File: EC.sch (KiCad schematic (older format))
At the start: 28 parts, among them J10 RS232, J2 MICROSD, J6 DEBUG, J8 DEBUG, Q12 FK3303010L, Q13 FK3303010L, SW3 SW-DIP-4, U10 MAX3232PW, U9 NUF2042XV6

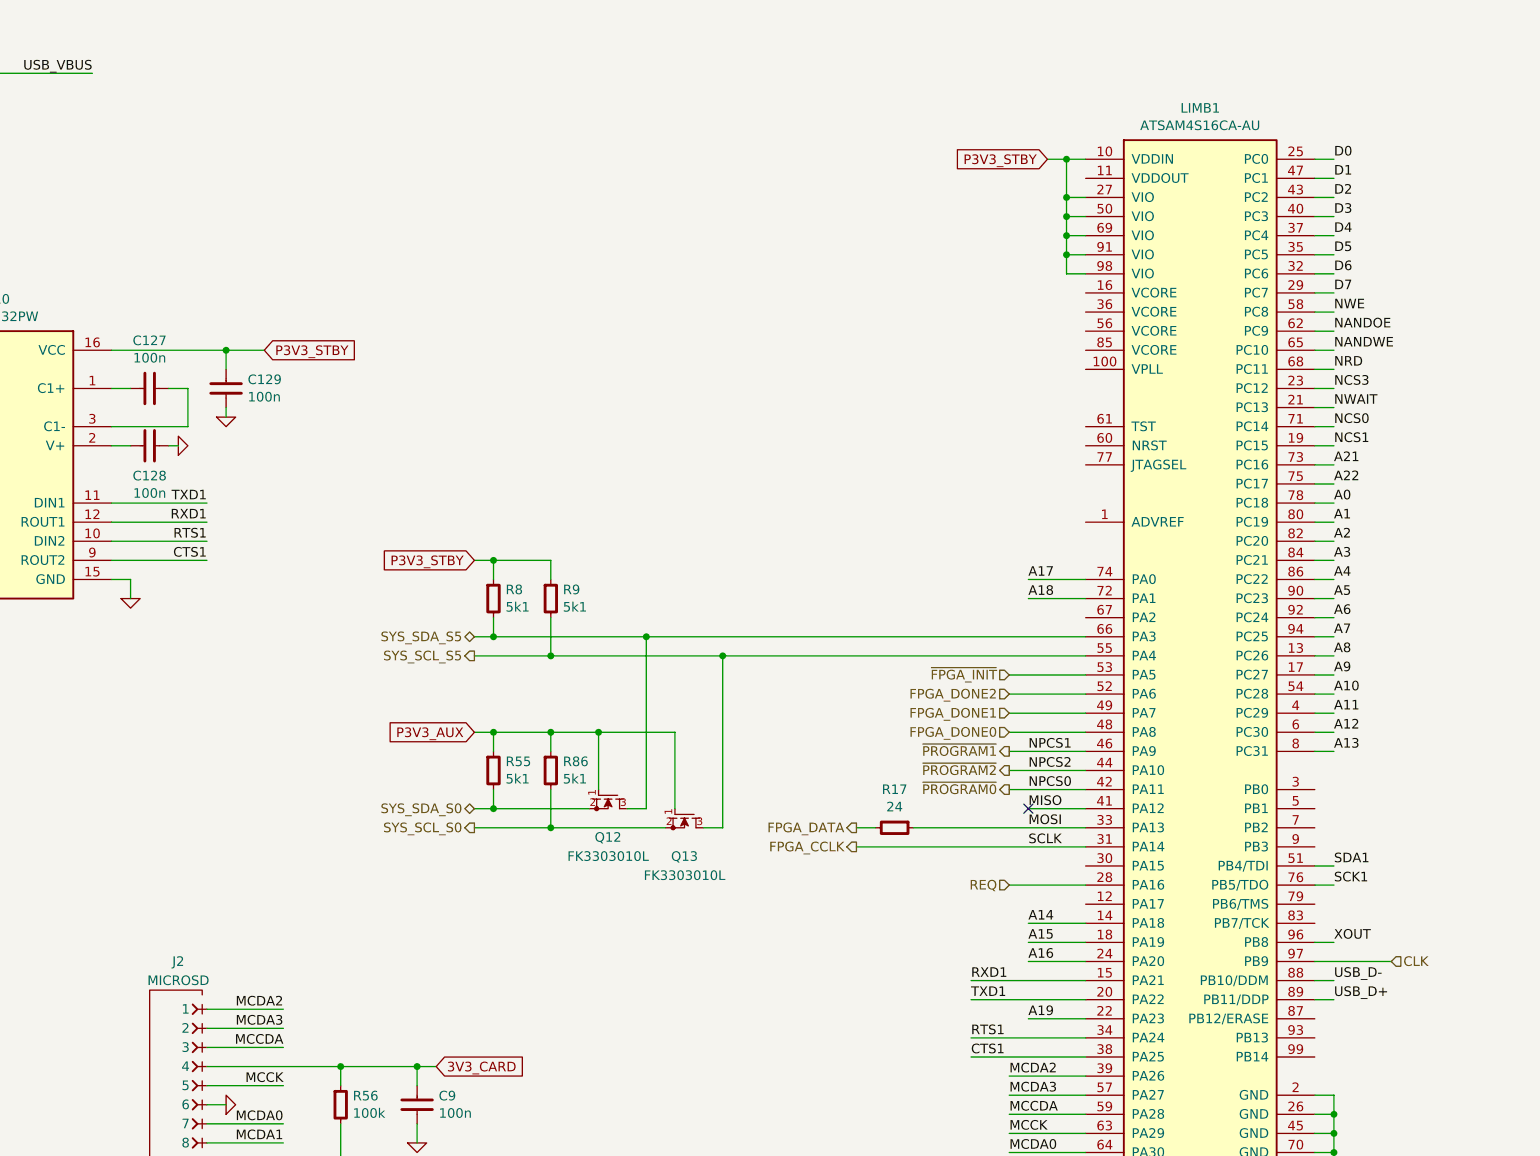
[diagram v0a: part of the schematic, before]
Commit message: Add CPU fan
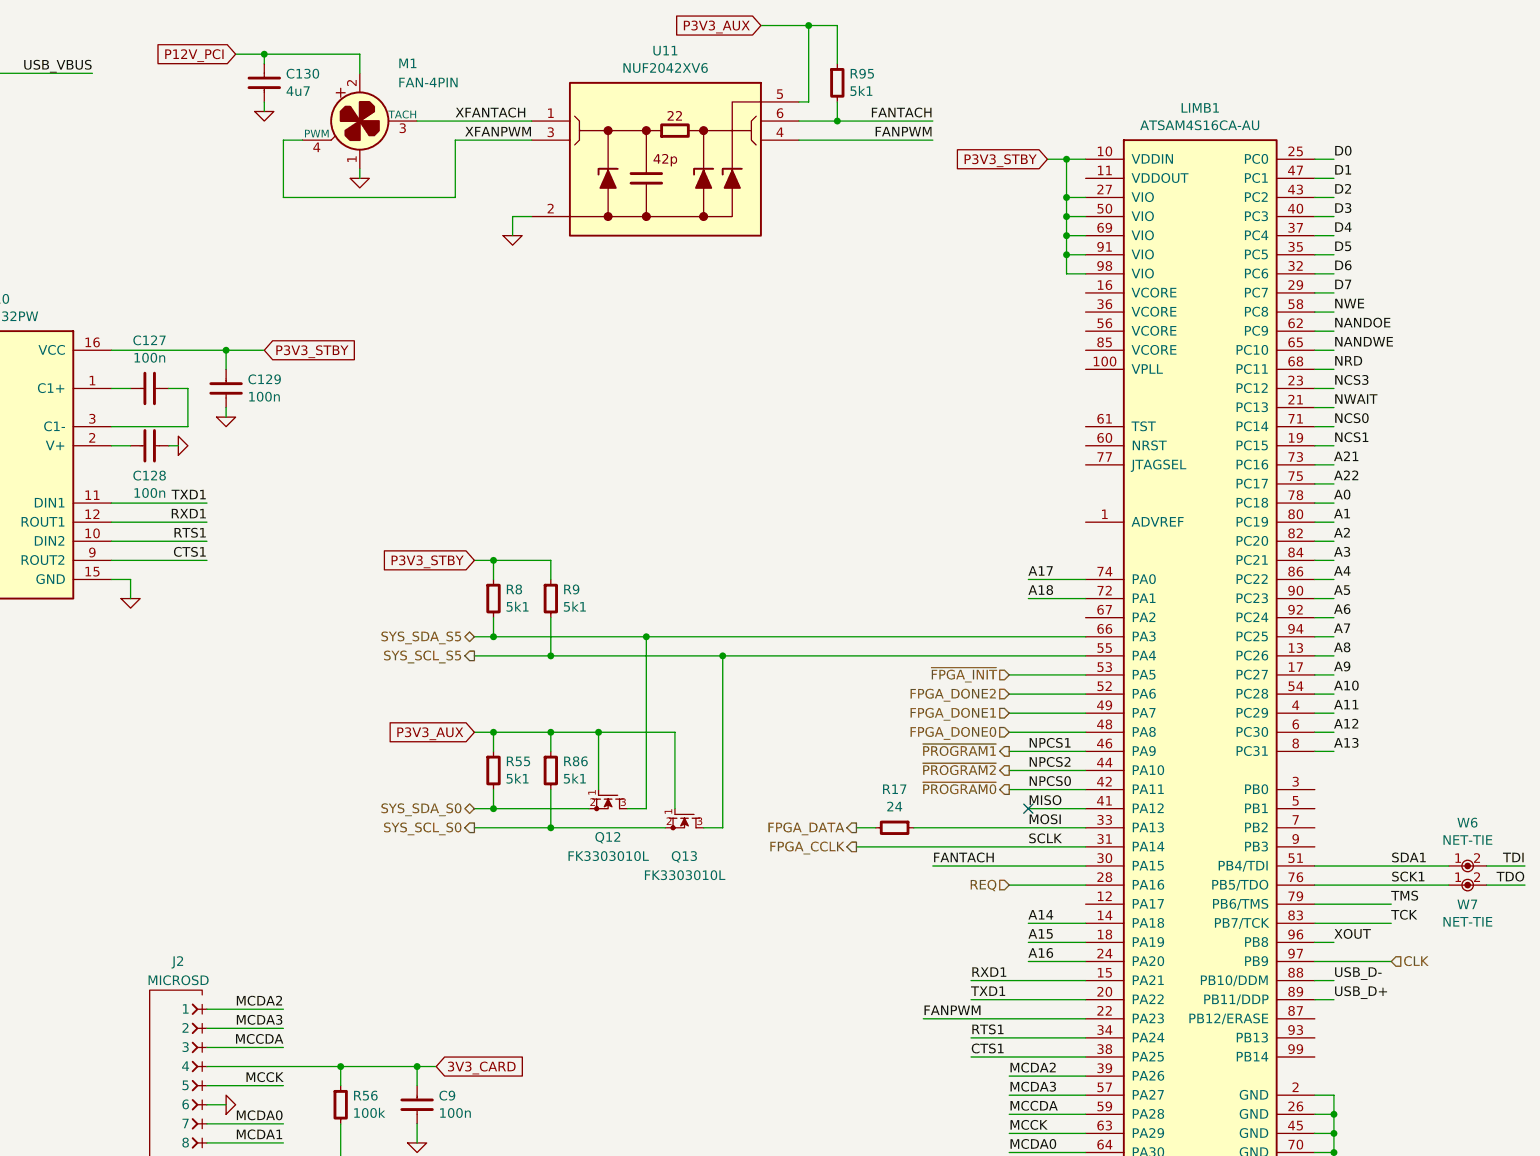
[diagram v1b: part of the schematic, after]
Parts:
- added C130: 4u7, IPC7351-Nominal:CAPC3216X70, symbol C-1206
- added M1: FAN-4PIN, conn-100mil:CONN-100MIL-M-1x4-SHROUD, symbol FAN-4PIN
- added R95: 5k1, IPC7351-Nominal:RESC1005X40, symbol R-0402
- added U11: NUF2042XV6, smd-semi:SOT-563, symbol NUF2042XV6
- added W6, W7: NET-TIE, conn-test:NET-TIE-0.2mm, symbol NET-TIE
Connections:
- net labels added: FANPWM, FANTACH, P12V_PCI, XFANPWM, XFANTACH
- net labels removed: A19
- wire segments 191 -> 216
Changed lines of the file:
@@
 Text Label 9000 3700 0    50   ~ 0
 A18
-Text Label 9000 5900 0    50   ~ 0
-A19
 Text Label 10600 3000 0    50   ~ 0
 A21
@@
 Text Label 8900 6300 0    50   ~ 0
 MCDA3
-Text Label 10600 5200 0    50   ~ 0
+Text Label 10900 5200 0    50   ~ 0
 SCK1
-Text Label 10600 5100 0    50   ~ 0
+Text Label 10900 5100 0    50   ~ 0
 SDA1
 Text Label 10600 5800 0    50   ~ 0
@@
 	8700 5800 9300 5800
 Wire Wire Line
-	9000 5900 9300 5900
+	8450 5900 9300 5900
 Wire Wire Line
 	8700 6000 9300 6000
@@
 	10500 4500 10600 4500
 Wire Wire Line
-	10500 5100 10600 5100
-Wire Wire Line
-	10500 5200 10600 5200
+	10500 5100 11200 5100
+Wire Wire Line
+	10500 5200 11200 5200
 Wire Wire Line
 	10600 5500 10500 5500
@@
 	10600 5800 10500 5800
 $Comp
-L GND #PWR137
+L GND #PWR140
 U 1 1 577EAB82
 P 10600 6800
-F 0 "#PWR137" H 10600 6800 30  0001 C CNN
+F 0 "#PWR140" H 10600 6800 30  0001 C CNN
 F 1 "GND" H 10600 6730 30  0001 C CNN
 F 2 "" H 10600 6800 60  0000 C CNN
@@
 Connection ~ 5800 6150
 $Comp
-L GND #PWR136
+L GND #PWR138
 U 1 1 577EEC84
 P 5800 6550
-F 0 "#PWR136" H 5800 6550 30  0001 C CNN
+F 0 "#PWR138" H 5800 6550 30  0001 C CNN
 F 1 "GND" H 5800 6480 30  0001 C CNN
 F 2 "" H 5800 6550 60  0000 C CNN
@@
 Wire Wire Line
 	4200 3400 4700 3400
+$Comp
+L NET-TIE W6
+U 1 1 57A3DAE4
+P 11300 5100
+F 0 "W6" H 11300 5325 50  0000 C CNN
+F 1 "NET-TIE" H 11300 5234 50  0000 C CNN
+F 2 "conn-test:NET-TIE-0.2mm" H 11300 5000 50  0001 C CNN
+F 3 "" H 11300 5100 60  0000 C CNN
+	1    11300 5100
+	1    0    0    -1
+$EndComp
+Text Label 11600 5100 2    50   ~ 0
+TDI
+Wire Wire Line
+	11600 5100 11400 5100
+$Comp
+L NET-TIE W7
+U 1 1 57A3DF12
+P 11300 5200
+F 0 "W7" H 11300 5097 50  0000 C CNN
+F 1 "NET-TIE" H 11300 5006 50  0000 C CNN
+F 2 "conn-test:NET-TIE-0.2mm" H 11300 5100 50  0001 C CNN
+F 3 "" H 11300 5200 60  0000 C CNN
+	1    11300 5200
+	1    0    0    -1
+$EndComp
+Text Label 11600 5200 2    50   ~ 0
+TDO
+Wire Wire Line
+	11600 5200 11400 5200
+Text Label 10900 5300 0    50   ~ 0
+TMS
+Wire Wire Line
+	10900 5300 10500 5300
+Text Label 10900 5400 0    50   ~ 0
+TCK
+Wire Wire Line
+	10900 5400 10500 5400
+$Comp
+L FAN-4PIN M1
+U 1 1 57A3FD69
+P 5500 1200
+F 0 "M1" H 5700 1500 50  0000 L CNN
+F 1 "FAN-4PIN" H 5700 1400 50  0000 L CNN
+F 2 "conn-100mil:CONN-100MIL-M-1x4-SHROUD" H 5841 1109 60  0001 L CNN
+F 3 "" H 5500 1200 60  0000 C CNN
+	1    5500 1200
+	1    0    0    -1
+$EndComp
+$Comp
+L GND #PWR137
+U 1 1 57A3FEDE
+P 5500 1500
+F 0 "#PWR137" H 5500 1500 30  0001 C CNN
+F 1 "GND" H 5500 1430 30  0001 C CNN
+F 2 "" H 5500 1500 60  0000 C CNN
+F 3 "" H 5500 1500 60  0000 C CNN
+	1    5500 1500
+	1    0    0    -1
+$EndComp
+Wire Wire Line
+	5500 1500 5500 1450
+Wire Wire Line
+	5500 850  5500 950
+Text GLabel 4850 850  0    50   Input ~ 0
+P12V_PCI
+Wire Wire Line
+	4850 850  5500 850
+$Comp
+L NUF2042XV6 U11
+U 1 1 57A4186D
+P 7100 1400
+F 0 "U11" H 7100 1967 50  0000 C CNN
+F 1 "NUF2042XV6" H 7100 1876 50  0000 C CNN
+F 2 "smd-semi:SOT-563" H 7100 700 50  0001 C CNN
+F 3 "http://www.onsemi.com/pub_link/Collateral/NUF2030XV6-D.PDF" H 7100 900 50  0001 C CNN
+F 4 "IC ONSEMI NUF2042XV6" H 7100 800 60  0001 C CNN "BOM"
+	1    7100 1400
+	1    0    0    -1
+$EndComp
+Wire Wire Line
+	5800 1200 6400 1200
+Wire Wire Line
+	6400 1300 6000 1300
+Wire Wire Line
+	6000 1300 6000 1600
+Wire Wire Line
+	6000 1600 5100 1600
+Wire Wire Line
+	5100 1600 5100 1300
+Wire Wire Line
+	5100 1300 5200 1300
+$Comp
+L GND #PWR139
+U 1 1 57A41BDC
+P 6300 1800
+F 0 "#PWR139" H 6300 1800 30  0001 C CNN
+F 1 "GND" H 6300 1730 30  0001 C CNN
+F 2 "" H 6300 1800 60  0000 C CNN
+F 3 "" H 6300 1800 60  0000 C CNN
+	1    6300 1800
+	1    0    0    -1
+$EndComp
+Wire Wire Line
+	6300 1800 6300 1700
+Wire Wire Line
+	6300 1700 6400 1700
+Text Label 6000 1200 0    50   ~ 0
+XFANTACH
+Text Label 6050 1300 0    50   ~ 0
+XFANPWM
+Text Label 8500 1200 2    50   ~ 0
+FANTACH
+Wire Wire Line
+	7800 1200 8500 1200
+Text Label 8500 1300 2    50   ~ 0
+FANPWM
+Wire Wire Line
+	8500 1300 7800 1300
+$Comp
+L R-0402 R95
+U 1 1 57A4253F
+P 8000 1000
+F 0 "R95" H 8063 1046 50  0000 L CNN
+F 1 "5k1" H 8063 955 50  0000 L CNN
+F 2 "IPC7351-Nominal:RESC1005X40" H 8000 1000 50  0001 C CNN
+F 3 "" H 8000 1050 60  0000 C CNN
+F 4 "RES SMD 5k1 1% [0402]" H 8750 1550 60  0001 C CNN "BOM"
+	1    8000 1000
+	1    0    0    -1
+$EndComp
+Wire Wire Line
+	8000 1100 8000 1200
+Connection ~ 8000 1200
+Text GLabel 7600 700  0    50   Input ~ 0
+P3V3_AUX
+Wire Wire Line
+	7600 700  8000 700
+Wire Wire Line
+	8000 700  8000 900
+Wire Wire Line
+	7850 700  7850 1100
+Wire Wire Line
+	7850 1100 7800 1100
+Connection ~ 7850 700
+$Comp
+L C-1206 C130
+U 1 1 57A49A02
+P 5000 1000
+F 0 "C130" H 5113 1046 50  0000 L CNN
+F 1 "4u7" H 5113 955 50  0000 L CNN
+F 2 "IPC7351-Nominal:CAPC3216X70" H 5000 1000 50  0001 C CNN
+F 3 "" H 4990 975 60  0000 C CNN
+F 4 "CAP MLCC 4u7 ≥X5R 25V 20% [1206]" H 5800 1550 60  0001 C CNN "BOM"
+	1    5000 1000
+	1    0    0    -1
+$EndComp
+Wire Wire Line
+	5000 900  5000 850
+Connection ~ 5000 850
+$Comp
+L GND #PWR136
+U 1 1 57A49C3C
+P 5000 1150
+F 0 "#PWR136" H 5000 1150 30  0001 C CNN
+F 1 "GND" H 5000 1080 30  0001 C CNN
+F 2 "" H 5000 1150 60  0000 C CNN
+F 3 "" H 5000 1150 60  0000 C CNN
+	1    5000 1150
+	1    0    0    -1
+$EndComp
+Wire Wire Line
+	5000 1150 5000 1100
+Text Label 8450 5900 0    50   ~ 0
+FANPWM
+Text Label 8500 5100 0    50   ~ 0
+FANTACH
+Wire Wire Line
+	8500 5100 9300 5100
 $EndSCHEMATC

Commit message: Add SDRAM SPD to I2C
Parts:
- M1: BOM (none) -> DIST DIGIKEY WM4330-ND
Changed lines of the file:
@@
 F 2 "conn-100mil:CONN-100MIL-M-1x4-SHROUD" H 5841 1109 60  0001 L CNN
 F 3 "" H 5500 1200 60  0000 C CNN
+F 4 "DIST DIGIKEY WM4330-ND" H 5500 1200 60  0001 C CNN "BOM"
 	1    5500 1200
 	1    0    0    -1

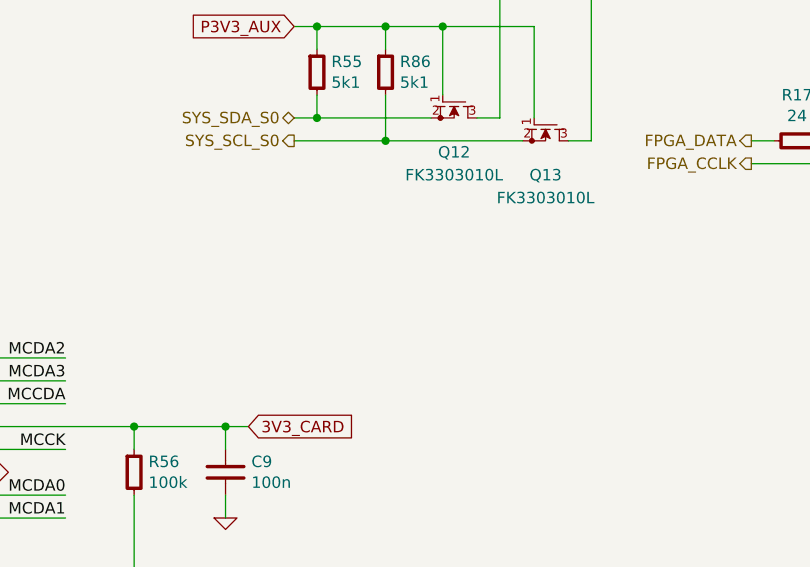
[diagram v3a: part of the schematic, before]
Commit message: Route PCI SMBUS
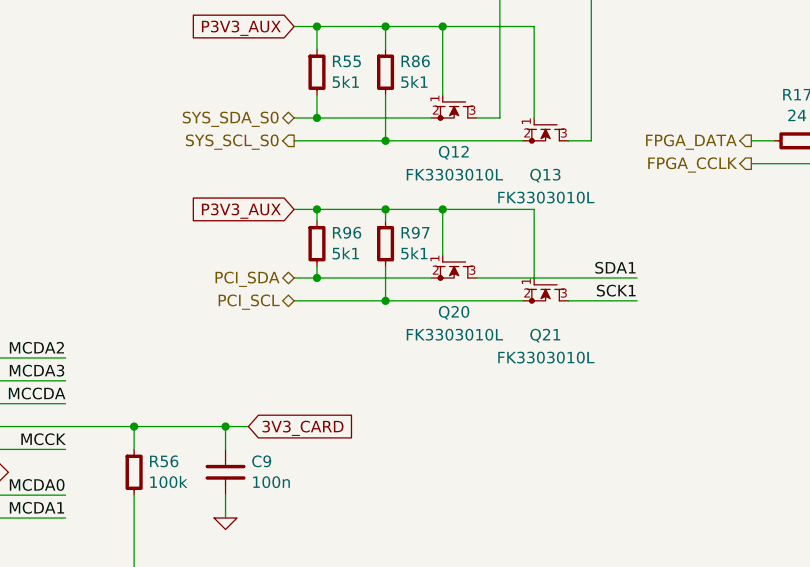
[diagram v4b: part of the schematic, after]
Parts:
- added Q20, Q21: FK3303010L, manuf:PANASONIC-SSSMini3-F2-B, symbol FK3303010L
- added R96, R97: 5k1, IPC7351-Nominal:RESC1005X40, symbol R-0402
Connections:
- net labels added: PCI_SCL, PCI_SDA
- wire segments 216 -> 227
